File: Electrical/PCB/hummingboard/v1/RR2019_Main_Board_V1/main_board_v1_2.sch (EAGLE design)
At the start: 143 parts, among them CN1 MIRCO_B, IC1 OR_SC70-5, J10 I2C_5V_4, J11 SERVO_LEFT, J12 SERVO_RIGHT, J13 ESC, J14 5V_INPUT, J15 QUAD_ENCODER_2, J16 7.2V_INPUT, J17 I2C_5V_FXIO_1, J18 I2C_5V_FXIO_2, J19 JETSON_TRIGGER, J2 REAR_ENCODER, J20 QUAD_ENCODER_1, J21 BLDC_HALL, J22 SPI_FXIO_1, J3 FRONT_ENCODER, J4 I2C_1V8_1, J5 SPI_2, J6 WIRELESS_MODULE, J7 UART_0, J8 UART_2, J9 STEERING_ANGLE, Q1 BSS138, Q3 DMP2066LSN, Q4 BSS138, Q5 BSS138, Q6 BSS138, Q7 BSS138, Q8 BSS138, U3 ICM-20948, U4 PCA9306

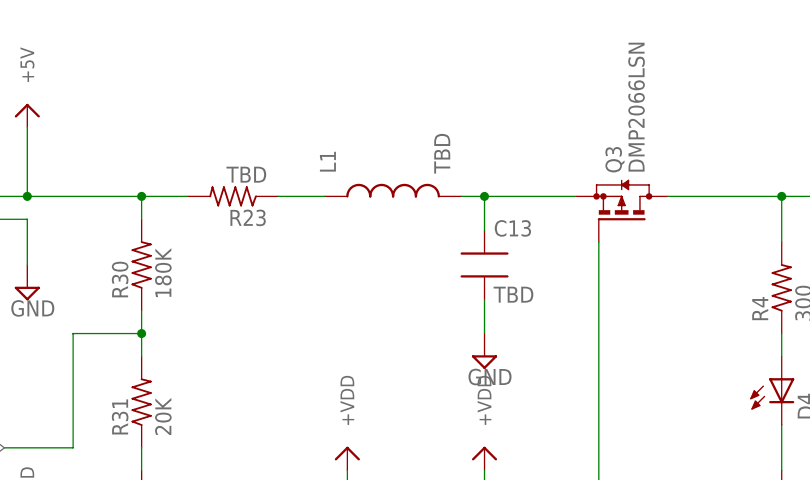
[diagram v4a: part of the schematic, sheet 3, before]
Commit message: add filter values
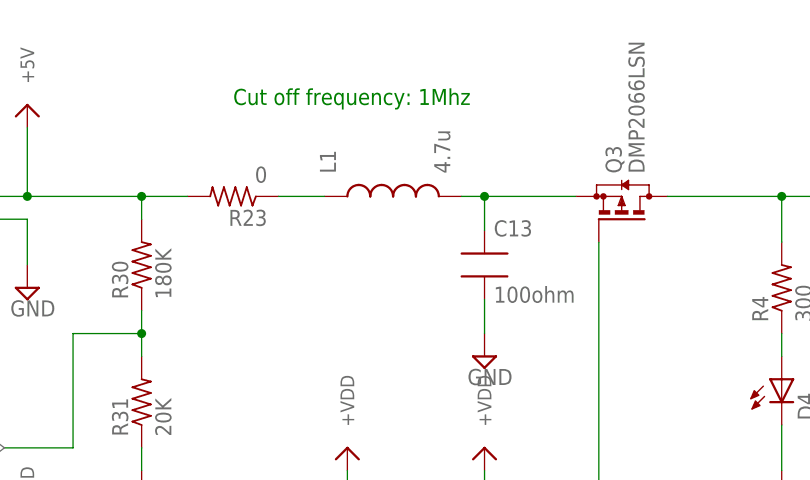
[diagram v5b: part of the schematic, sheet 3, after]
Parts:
- C13: value TBD -> 100ohm
- L1: value TBD -> 4.7u
- R23: value TBD -> 0
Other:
- note added: "Cut off frequency: 1Mhz"
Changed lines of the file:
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@@
 <part name="D4" library="RobotRacing2019_Master" deviceset="LED0603" device="" value="LED_GREEN"/>
 <part name="Q3" library="RobotRacing2019_Master" deviceset="PMOS_SOT23" device="" value="DMP2066LSN"/>
-<part name="C13" library="RobotRacing2019_Master" deviceset="CAP0603" device="" value="TBD"/>
-<part name="L1" library="RobotRacing2019_Master" deviceset="IND0603" device="" value="TBD"/>
+<part name="C13" library="RobotRacing2019_Master" deviceset="CAP0603" device="" value="100ohm"/>
+<part name="L1" library="RobotRacing2019_Master" deviceset="IND0603" device="" value="4.7u"/>
 <part name="C17" library="RobotRacing2019_Master" deviceset="CAP0603" device="" value="0.1uF">
 <attribute name="SPICEPREFIX" value="C"/>
@@
 <part name="J14" library="RobotRacing2019_Master" deviceset="PINHEAD-2-VERTICAL" device="" value="5V_INPUT"/>
 <part name="SUPPLY43" library="RobotRacing2019_Master" deviceset="GND" device=""/>
-<part name="R23" library="RobotRacing2019_Master" deviceset="RES0603" device="" value="TBD"/>
+<part name="R23" library="RobotRacing2019_Master" deviceset="RES0603" device="" value="0"/>
 <part name="U$35" library="RobotRacing2019_Master" deviceset="+VDD" device=""/>
 <part name="R24" library="RobotRacing2019_Master" deviceset="RES0603" device="" value="100K"/>
@@
 <text x="-10.16" y="15.24" size="1.778" layer="97">5V - 3.3 V LDO </text>
 <text x="-7.62" y="-30.48" size="1.778" layer="97">5V - 1.8 V LDO </text>
+<text x="-114.3" y="15.24" size="1.778" layer="91">Cut off frequency: 1Mhz</text>
 </plain>
 <instances>

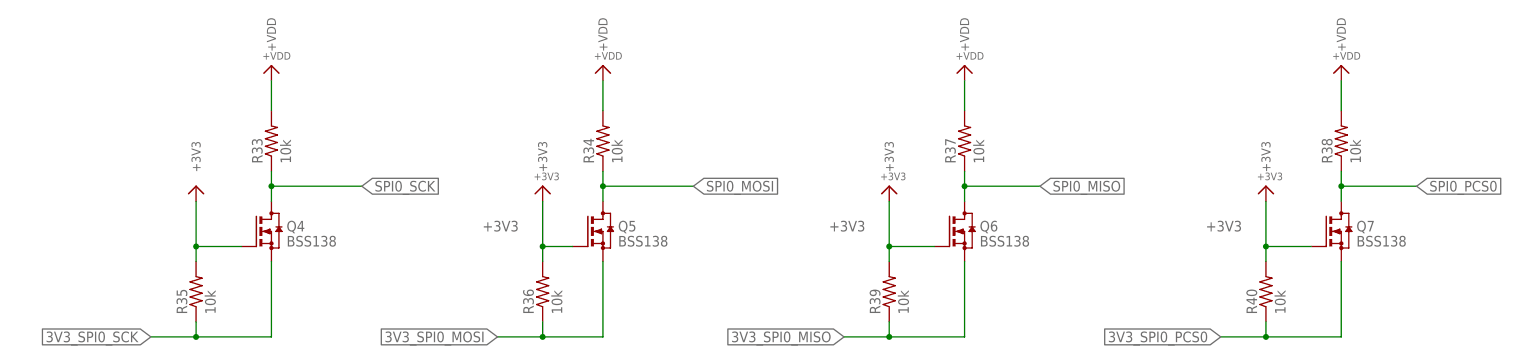
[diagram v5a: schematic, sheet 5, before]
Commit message: fix the MOSI/MISO direction
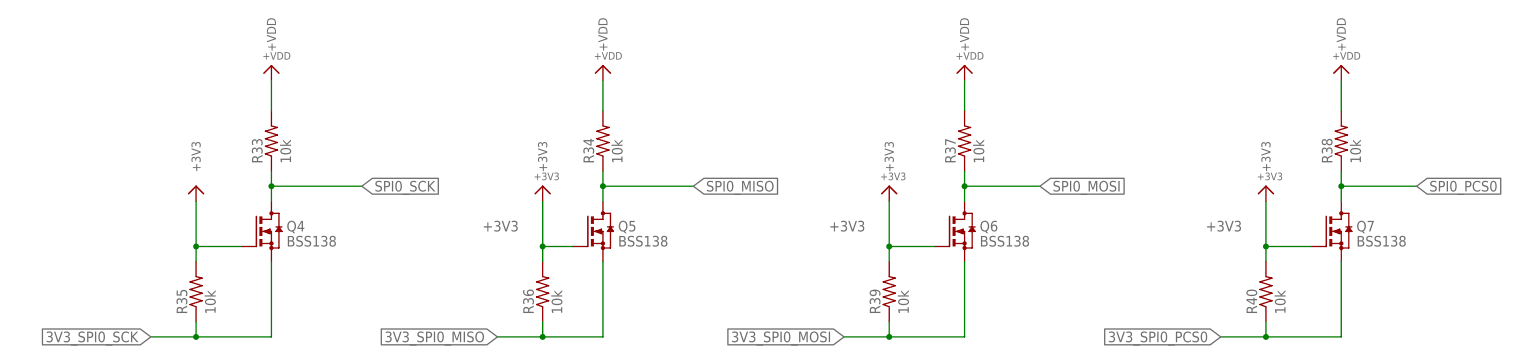
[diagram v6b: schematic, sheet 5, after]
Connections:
- net 3V3_SPI0_MISO: now also J6.4, Q5.S, R36.1; no longer J6.5, Q6.S, R39.1
- net 3V3_SPI0_MOSI: now also J6.5, Q6.S, R39.1; no longer J6.4, Q5.S, R36.1
- net SPI0_MISO: now also J5.4, Q5.D, R34.1, U$1.PTE1; no longer J5.5, Q6.D, R37.1, U$1.PTE2
- net SPI0_MOSI: now also J5.5, Q6.D, R37.1, U$1.PTE2; no longer J5.4, Q5.D, R34.1, U$1.PTE1
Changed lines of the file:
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@@
 <net name="SPI0_MISO" class="0">
-<segment>
-<pinref part="U$1" gate="G$1" pin="PTE2"/>
-<wire x1="7.62" y1="45.72" x2="7.62" y2="48.26" width="0.1524" layer="91"/>
-<label x="7.62" y="48.26" size="1.778" layer="95" rot="R90" xref="yes"/>
-</segment>
-</net>
-<net name="SPI0_MOSI" class="0">
 <segment>
 <pinref part="U$1" gate="G$1" pin="PTE1"/>
@@
 <pinref part="U$4" gate="G$1" pin="+VDD"/>
 <label x="-185.42" y="7.62" size="1.778" layer="95"/>
+</segment>
+</net>
+<net name="SPI0_MOSI" class="0">
+<segment>
+<pinref part="U$1" gate="G$1" pin="PTE2"/>
+<wire x1="7.62" y1="45.72" x2="7.62" y2="48.26" width="0.1524" layer="91"/>
+<label x="7.62" y="48.26" size="1.778" layer="95" rot="R90" xref="yes"/>
 </segment>
 </net>
@@
 </segment>
 </net>
-<net name="SPI0_MOSI" class="0">
+<net name="SPI0_MISO" class="0">
 <segment>
 <pinref part="Q5" gate="G$1" pin="D"/>
@@
 </segment>
 </net>
-<net name="3V3_SPI0_MOSI" class="0">
+<net name="3V3_SPI0_MISO" class="0">
 <segment>
 <pinref part="Q5" gate="G$1" pin="S"/>
@@
 </segment>
 </net>
-<net name="SPI0_MISO" class="0">
-<segment>
-<pinref part="R37" gate="G$1" pin="1"/>
-<pinref part="Q6" gate="G$1" pin="D"/>
-<label x="48.26" y="10.16" size="1.778" layer="95" xref="yes"/>
-<wire x1="35.56" y1="12.7" x2="35.56" y2="10.16" width="0.1524" layer="91"/>
-<wire x1="35.56" y1="10.16" x2="35.56" y2="7.62" width="0.1524" layer="91"/>
-<wire x1="48.26" y1="10.16" x2="35.56" y2="10.16" width="0.1524" layer="91"/>
-<junction x="35.56" y="10.16"/>
-</segment>
-</net>
-<net name="3V3_SPI0_MISO" class="0">
+<net name="SPI0_PCS0" class="0">
+<segment>
+<pinref part="R38" gate="G$1" pin="1"/>
+<pinref part="Q7" gate="G$1" pin="D"/>
+<label x="111.76" y="10.16" size="1.778" layer="95" xref="yes"/>
+<wire x1="99.06" y1="12.7" x2="99.06" y2="10.16" width="0.1524" layer="91"/>
+<wire x1="99.06" y1="10.16" x2="99.06" y2="7.62" width="0.1524" layer="91"/>
+<wire x1="111.76" y1="10.16" x2="99.06" y2="10.16" width="0.1524" layer="91"/>
+<junction x="99.06" y="10.16"/>
+</segment>
+</net>
+<net name="3V3_SPI0_PCS0" class="0">
+<segment>
+<pinref part="Q7" gate="G$1" pin="S"/>
+<wire x1="99.06" y1="-2.54" x2="99.06" y2="-15.24" width="0.1524" layer="91"/>
+<wire x1="99.06" y1="-15.24" x2="86.36" y2="-15.24" width="0.1524" layer="91"/>
+<pinref part="R40" gate="G$1" pin="1"/>
+<wire x1="86.36" y1="-15.24" x2="78.74" y2="-15.24" width="0.1524" layer="91"/>
+<wire x1="86.36" y1="-12.7" x2="86.36" y2="-15.24" width="0.1524" layer="91"/>
+<junction x="86.36" y="-15.24"/>
+<label x="78.74" y="-15.24" size="1.778" layer="95" rot="R180" xref="yes"/>
+</segment>
+</net>
+<net name="+3V3" class="0">
+<segment>
+<pinref part="Q4" gate="G$1" pin="G"/>
+<wire x1="-86.36" y1="0" x2="-93.98" y2="0" width="0.1524" layer="91"/>
+<wire x1="-93.98" y1="0" x2="-93.98" y2="7.62" width="0.1524" layer="91"/>
+<pinref part="R35" gate="G$1" pin="2"/>
+<wire x1="-93.98" y1="0" x2="-93.98" y2="-2.54" width="0.1524" layer="91"/>
+<junction x="-93.98" y="0"/>
+<pinref part="U$52" gate="G$1" pin="+3V3"/>
+</segment>
+<segment>
+<pinref part="Q5" gate="G$1" pin="G"/>
+<wire x1="-30.48" y1="0" x2="-35.56" y2="0" width="0.1524" layer="91"/>
+<wire x1="-35.56" y1="7.62" x2="-35.56" y2="0" width="0.1524" layer="91"/>
+<pinref part="R36" gate="G$1" pin="2"/>
+<wire x1="-35.56" y1="0" x2="-35.56" y2="-2.54" width="0.1524" layer="91"/>
+<junction x="-35.56" y="0"/>
+<pinref part="U$53" gate="G$1" pin="+3V3"/>
+<label x="-45.72" y="2.54" size="1.778" layer="95"/>
+</segment>
+<segment>
+<pinref part="Q6" gate="G$1" pin="G"/>
+<wire x1="30.48" y1="0" x2="22.86" y2="0" width="0.1524" layer="91"/>
+<wire x1="22.86" y1="0" x2="22.86" y2="7.62" width="0.1524" layer="91"/>
+<pinref part="R39" gate="G$1" pin="2"/>
+<wire x1="22.86" y1="0" x2="22.86" y2="-2.54" width="0.1524" layer="91"/>
+<junction x="22.86" y="0"/>
+<pinref part="U$56" gate="G$1" pin="+3V3"/>
+<label x="12.7" y="2.54" size="1.778" layer="95"/>
+</segment>
+<segment>
+<pinref part="Q7" gate="G$1" pin="G"/>
+<wire x1="93.98" y1="0" x2="86.36" y2="0" width="0.1524" layer="91"/>
+<wire x1="86.36" y1="0" x2="86.36" y2="7.62" width="0.1524" layer="91"/>
+<pinref part="R40" gate="G$1" pin="2"/>
+<wire x1="86.36" y1="0" x2="86.36" y2="-2.54" width="0.1524" layer="91"/>
+<junction x="86.36" y="0"/>
+<pinref part="U$57" gate="G$1" pin="+3V3"/>
+<label x="76.2" y="2.54" size="1.778" layer="95"/>
+</segment>
+</net>
+<net name="3V3_SPI0_MOSI" class="0">
 <segment>
 <pinref part="Q6" gate="G$1" pin="S"/>
@@
 </segment>
 </net>
-<net name="SPI0_PCS0" class="0">
-<segment>
-<pinref part="R38" gate="G$1" pin="1"/>
-<pinref part="Q7" gate="G$1" pin="D"/>
-<label x="111.76" y="10.16" size="1.778" layer="95" xref="yes"/>
-<wire x1="99.06" y1="12.7" x2="99.06" y2="10.16" width="0.1524" layer="91"/>
-<wire x1="99.06" y1="10.16" x2="99.06" y2="7.62" width="0.1524" layer="91"/>
-<wire x1="111.76" y1="10.16" x2="99.06" y2="10.16" width="0.1524" layer="91"/>
-<junction x="99.06" y="10.16"/>
-</segment>
-</net>
-<net name="3V3_SPI0_PCS0" class="0">
-<segment>
-<pinref part="Q7" gate="G$1" pin="S"/>
-<wire x1="99.06" y1="-2.54" x2="99.06" y2="-15.24" width="0.1524" layer="91"/>
-<wire x1="99.06" y1="-15.24" x2="86.36" y2="-15.24" width="0.1524" layer="91"/>
-<pinref part="R40" gate="G$1" pin="1"/>
-<wire x1="86.36" y1="-15.24" x2="78.74" y2="-15.24" width="0.1524" layer="91"/>
-<wire x1="86.36" y1="-12.7" x2="86.36" y2="-15.24" width="0.1524" layer="91"/>
-<junction x="86.36" y="-15.24"/>
-<label x="78.74" y="-15.24" size="1.778" layer="95" rot="R180" xref="yes"/>
-</segment>
-</net>
-<net name="+3V3" class="0">
-<segment>
-<pinref part="Q4" gate="G$1" pin="G"/>
-<wire x1="-86.36" y1="0" x2="-93.98" y2="0" width="0.1524" layer="91"/>
-<wire x1="-93.98" y1="0" x2="-93.98" y2="7.62" width="0.1524" layer="91"/>
-<pinref part="R35" gate="G$1" pin="2"/>
-<wire x1="-93.98" y1="0" x2="-93.98" y2="-2.54" width="0.1524" layer="91"/>
-<junction x="-93.98" y="0"/>
-<pinref part="U$52" gate="G$1" pin="+3V3"/>
-</segment>
-<segment>
-<pinref part="Q5" gate="G$1" pin="G"/>
-<wire x1="-30.48" y1="0" x2="-35.56" y2="0" width="0.1524" layer="91"/>
-<wire x1="-35.56" y1="7.62" x2="-35.56" y2="0" width="0.1524" layer="91"/>
-<pinref part="R36" gate="G$1" pin="2"/>
-<wire x1="-35.56" y1="0" x2="-35.56" y2="-2.54" width="0.1524" layer="91"/>
-<junction x="-35.56" y="0"/>
-<pinref part="U$53" gate="G$1" pin="+3V3"/>
-<label x="-45.72" y="2.54" size="1.778" layer="95"/>
-</segment>
-<segment>
-<pinref part="Q6" gate="G$1" pin="G"/>
-<wire x1="30.48" y1="0" x2="22.86" y2="0" width="0.1524" layer="91"/>
-<wire x1="22.86" y1="0" x2="22.86" y2="7.62" width="0.1524" layer="91"/>
-<pinref part="R39" gate="G$1" pin="2"/>
-<wire x1="22.86" y1="0" x2="22.86" y2="-2.54" width="0.1524" layer="91"/>
-<junction x="22.86" y="0"/>
-<pinref part="U$56" gate="G$1" pin="+3V3"/>
-<label x="12.7" y="2.54" size="1.778" layer="95"/>
-</segment>
-<segment>
-<pinref part="Q7" gate="G$1" pin="G"/>
-<wire x1="93.98" y1="0" x2="86.36" y2="0" width="0.1524" layer="91"/>
-<wire x1="86.36" y1="0" x2="86.36" y2="7.62" width="0.1524" layer="91"/>
-<pinref part="R40" gate="G$1" pin="2"/>
-<wire x1="86.36" y1="0" x2="86.36" y2="-2.54" width="0.1524" layer="91"/>
-<junction x="86.36" y="0"/>
-<pinref part="U$57" gate="G$1" pin="+3V3"/>
-<label x="76.2" y="2.54" size="1.778" layer="95"/>
+<net name="SPI0_MOSI" class="0">
+<segment>
+<pinref part="R37" gate="G$1" pin="1"/>
+<pinref part="Q6" gate="G$1" pin="D"/>
+<label x="48.26" y="10.16" size="1.778" layer="95" xref="yes"/>
+<wire x1="35.56" y1="12.7" x2="35.56" y2="10.16" width="0.1524" layer="91"/>
+<wire x1="35.56" y1="10.16" x2="35.56" y2="7.62" width="0.1524" layer="91"/>
+<wire x1="48.26" y1="10.16" x2="35.56" y2="10.16" width="0.1524" layer="91"/>
+<junction x="35.56" y="10.16"/>
 </segment>
 </net>
@@
 <net name="3V3_SPI0_MOSI" class="0">
 <segment>
-<wire x1="-33.02" y1="25.4" x2="-10.16" y2="25.4" width="0.1524" layer="91"/>
-<wire x1="-10.16" y1="25.4" x2="-10.16" y2="40.64" width="0.1524" layer="91"/>
-<label x="-10.16" y="40.64" size="1.778" layer="95" rot="R90" xref="yes"/>
-<pinref part="J6" gate="G$1" pin="4"/>
-</segment>
-</net>
-<net name="3V3_SPI0_MISO" class="0">
-<segment>
 <wire x1="-33.02" y1="22.86" x2="-5.08" y2="22.86" width="0.1524" layer="91"/>
 <wire x1="-5.08" y1="22.86" x2="-5.08" y2="40.64" width="0.1524" layer="91"/>
@@
 </segment>
 </net>
-<net name="SPI0_MISO" class="0">
+<net name="SPI0_MOSI" class="0">
 <segment>
 <wire x1="7.62" y1="22.86" x2="7.62" y2="40.64" width="0.1524" layer="91"/>
@@
 <pinref part="J5" gate="G$1" pin="5"/>
 <wire x1="7.62" y1="22.86" x2="40.64" y2="22.86" width="0.1524" layer="91"/>
-</segment>
-</net>
-<net name="SPI0_MOSI" class="0">
-<segment>
-<wire x1="12.7" y1="25.4" x2="12.7" y2="40.64" width="0.1524" layer="91"/>
-<label x="12.7" y="40.64" size="1.778" layer="95" rot="R90" xref="yes"/>
-<pinref part="J5" gate="G$1" pin="4"/>
-<wire x1="40.64" y1="25.4" x2="12.7" y2="25.4" width="0.1524" layer="91"/>
 </segment>
 </net>
@@
 </segment>
 </net>
+<net name="SPI0_MISO" class="0">
+<segment>
+<wire x1="12.7" y1="25.4" x2="12.7" y2="40.64" width="0.1524" layer="91"/>
+<label x="12.7" y="40.64" size="1.778" layer="95" rot="R90" xref="yes"/>
+<pinref part="J5" gate="G$1" pin="4"/>
+<wire x1="40.64" y1="25.4" x2="12.7" y2="25.4" width="0.1524" layer="91"/>
+</segment>
+</net>
+<net name="3V3_SPI0_MISO" class="0">
+<segment>
+<wire x1="-33.02" y1="25.4" x2="-10.16" y2="25.4" width="0.1524" layer="91"/>
+<wire x1="-10.16" y1="25.4" x2="-10.16" y2="40.64" width="0.1524" layer="91"/>
+<label x="-10.16" y="40.64" size="1.778" layer="95" rot="R90" xref="yes"/>
+<pinref part="J6" gate="G$1" pin="4"/>
+</segment>
+</net>
